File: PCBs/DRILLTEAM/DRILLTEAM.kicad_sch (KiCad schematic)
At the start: 84 parts, among them J10 Conn_01x04, J11 Conn_01x08, J12 Conn_01x04, J13 TYPE-C-31-M-12, J2 Conn_01x02, J3 Conn_01x03, J4 Conn_01x03, J5 Conn_01x04, J6 Conn_01x04, J7 Conn_01x02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

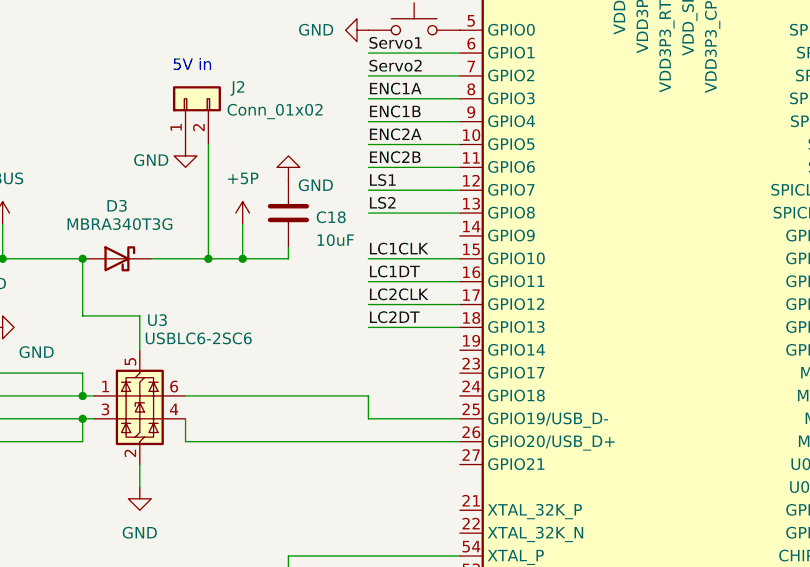
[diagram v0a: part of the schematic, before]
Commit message: Finished PCB sub mounting holes and fillet
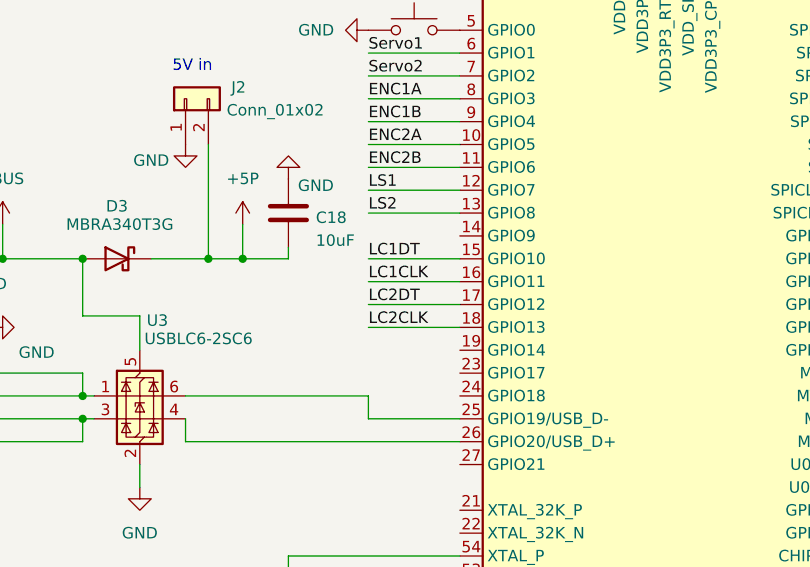
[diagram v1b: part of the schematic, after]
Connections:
- net LC1CLK: now also U1.16 (GPIO11); no longer U1.15 (GPIO10)
- net LC1DT: now also U1.15 (GPIO10); no longer U1.16 (GPIO11)
- net LC2CLK: now also U1.18 (GPIO13); no longer U1.17 (GPIO12)
- net LC2DT: now also U1.17 (GPIO12); no longer U1.18 (GPIO13)
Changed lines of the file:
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@@
 	(wire
 		(pts
+			(xy 323.85 101.6) (xy 334.01 101.6)
+		)
+		(stroke
+			(width 0)
+			(type default)
+		)
+	)
+	(wire
+		(pts
 			(xy 46.99 219.71) (xy 55.88 219.71)
 		)
@@
 	(wire
 		(pts
+			(xy 323.85 93.98) (xy 334.01 93.98)
+		)
+		(stroke
+			(width 0)
+			(type default)
+		)
+	)
+	(wire
+		(pts
 			(xy 22.86 275.59) (xy 31.75 275.59)
 		)
@@
 	(wire
 		(pts
+			(xy 323.85 99.06) (xy 334.01 99.06)
+		)
+		(stroke
+			(width 0)
+			(type default)
+		)
+	)
+	(wire
+		(pts
 			(xy 166.37 162.56) (xy 166.37 157.48)
 		)
@@
 	(wire
 		(pts
-			(xy 323.85 96.52) (xy 334.01 96.52)
-		)
-		(stroke
-			(width 0)
-			(type default)
-		)
-	)
-	(wire
-		(pts
 			(xy 190.5 154.94) (xy 190.5 152.4)
 		)
@@
 	(wire
 		(pts
-			(xy 323.85 99.06) (xy 334.01 99.06)
-		)
-		(stroke
-			(width 0)
-			(type default)
-		)
-	)
-	(wire
-		(pts
 			(xy 55.88 219.71) (xy 60.96 219.71)
 		)
@@
 	(wire
 		(pts
-			(xy 323.85 101.6) (xy 334.01 101.6)
-		)
-		(stroke
-			(width 0)
-			(type default)
-		)
-	)
-	(wire
-		(pts
 			(xy 48.26 147.32) (xy 45.72 147.32)
 		)
@@
 	(wire
 		(pts
-			(xy 323.85 93.98) (xy 334.01 93.98)
-		)
-		(stroke
-			(width 0)
-			(type default)
-		)
-	)
-	(wire
-		(pts
 			(xy 44.45 166.37) (xy 49.53 166.37)
 		)
@@
 	(wire
 		(pts
+			(xy 323.85 96.52) (xy 334.01 96.52)
+		)
+		(stroke
+			(width 0)
+			(type default)
+		)
+	)
+	(wire
+		(pts
 			(xy 193.04 146.05) (xy 176.53 146.05)
 		)
@@
 	)
 	(label "LC2DT"
-		(at 323.85 101.6 0)
+		(at 323.85 99.06 0)
 		(fields_autoplaced yes)
 		(effects
@@
 	)
 	(label "LC2CLK"
-		(at 323.85 99.06 0)
+		(at 323.85 101.6 0)
 		(fields_autoplaced yes)
 		(effects
@@
 	)
 	(label "LC1DT"
-		(at 323.85 96.52 0)
+		(at 323.85 93.98 0)
 		(fields_autoplaced yes)
 		(effects
@@
 	)
 	(label "LC1CLK"
-		(at 323.85 93.98 0)
+		(at 323.85 96.52 0)
 		(fields_autoplaced yes)
 		(effects

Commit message: Finished Drill PCB
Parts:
- added H1, H2, H3: MountingHole, MountingHole:MountingHole_3.2mm_M3, symbol Mechanical:MountingHole
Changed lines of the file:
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@@
 	)
 	(symbol
+		(lib_id "Mechanical:MountingHole")
+		(at 173.99 43.18 0)
+		(unit 1)
+		(exclude_from_sim yes)
+		(in_bom no)
+		(on_board yes)
+		(dnp no)
+		(fields_autoplaced yes)
+		(property "Reference" "H2"
+			(at 176.53 41.9099 0)
+			(effects
+				(font
+					(size 1.27 1.27)
+				)
+				(justify left)
+			)
+		)
+		(property "Value" "MountingHole"
+			(at 176.53 44.4499 0)
+			(effects
+				(font
+					(size 1.27 1.27)
+				)
+				(justify left)
+			)
+		)
+		(property "Footprint" "MountingHole:MountingHole_3.2mm_M3"
+			(at 173.99 43.18 0)
+			(effects
+				(font
+					(size 1.27 1.27)
+				)
+				(hide yes)
+			)
+		)
+		(property "Datasheet" "~"
+			(at 173.99 43.18 0)
+			(effects
+				(font
+					(size 1.27 1.27)
+				)
+				(hide yes)
+			)
+		)
+		(property "Description" "Mounting Hole without connection"
+			(at 173.99 43.18 0)
+			(effects
+				(font
+					(size 1.27 1.27)
+				)
+				(hide yes)
+			)
+		)
+		(instances
+			(project "DRILLTEAM"
+				(path "/b03f9be8-9d5f-4f70-bfa3-8e67a13f0ae1"
+					(reference "H2")
+					(unit 1)
+				)
+			)
+		)
+	)
+	(symbol
 		(lib_id "Device:C")
 		(at 123.19 226.06 0)
@@
 	)
 	(symbol
+		(lib_id "Mechanical:MountingHole")
+		(at 175.26 54.61 0)
+		(unit 1)
+		(exclude_from_sim yes)
+		(in_bom no)
+		(on_board yes)
+		(dnp no)
+		(fields_autoplaced yes)
+		(property "Reference" "H3"
+			(at 177.8 53.3399 0)
+			(effects
+				(font
+					(size 1.27 1.27)
+				)
+				(justify left)
+			)
+		)
+		(property "Value" "MountingHole"
+			(at 177.8 55.8799 0)
+			(effects
+				(font
+					(size 1.27 1.27)
+				)
+				(justify left)
+			)
+		)
+		(property "Footprint" "MountingHole:MountingHole_3.2mm_M3"
+			(at 175.26 54.61 0)
+			(effects
+				(font
+					(size 1.27 1.27)
+				)
+				(hide yes)
+			)
+		)
+		(property "Datasheet" "~"
+			(at 175.26 54.61 0)
+			(effects
+				(font
+					(size 1.27 1.27)
+				)
+				(hide yes)
+			)
+		)
+		(property "Description" "Mounting Hole without connection"
+			(at 175.26 54.61 0)
+			(effects
+				(font
+					(size 1.27 1.27)
+				)
+				(hide yes)
+			)
+		)
+		(instances
+			(project "DRILLTEAM"
+				(path "/b03f9be8-9d5f-4f70-bfa3-8e67a13f0ae1"
+					(reference "H3")
+					(unit 1)
+				)
+			)
+		)
+	)
+	(symbol
 		(lib_id "power:+5P")
 		(at 236.22 247.65 90)
@@
 					(unit 1)
 				)
+			)
+		)
+	)
+	(symbol
+		(lib_id "Mechanical:MountingHole")
+		(at 173.99 30.48 0)
+		(unit 1)
+		(exclude_from_sim yes)
+		(in_bom no)
+		(on_board yes)
+		(dnp no)
+		(fields_autoplaced yes)
+		(property "Reference" "H1"
+			(at 176.53 29.2099 0)
+			(effects
+				(font
+					(size 1.27 1.27)
+				)
+				(justify left)
+			)
+		)
+		(property "Value" "MountingHole"
+			(at 176.53 31.7499 0)
+			(effects
+				(font
+					(size 1.27 1.27)
+				)
+				(justify left)
+			)
+		)
+		(property "Footprint" "MountingHole:MountingHole_3.2mm_M3"
+			(at 173.99 30.48 0)
+			(effects
+				(font
+					(size 1.27 1.27)
+				)
+				(hide yes)
+			)
+		)
+		(property "Datasheet" "~"
+			(at 173.99 30.48 0)
+			(effects
+				(font
+					(size 1.27 1.27)
+				)
+				(hide yes)
+			)
+		)
+		(property "Description" "Mounting Hole without connection"
+			(at 173.99 30.48 0)
+			(effects
+				(font
+					(size 1.27 1.27)
+				)
+				(hide yes)
+			)
+		)
+		(instances
+			(project ""
+				(path "/b03f9be8-9d5f-4f70-bfa3-8e67a13f0ae1"
+					(reference "H1")
+					(unit 1)
+				)
